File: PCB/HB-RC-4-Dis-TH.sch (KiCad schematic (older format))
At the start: 41 parts, among them J1 FTDI, J2 SHT31, J3 eInk, J4 ISP, J5 Power, Q1 IRLML6346TRBPF, SW1 T1, SW2 T2, SW3 T3, SW4 T4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

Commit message: update pcb
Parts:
- J2: footprint Connector_PinHeader_2.00mm:PinHeader_1x04_P2.00mm_Vertical -> Connector_PinHeader_2.54mm:PinHeader_1x04_P2.54mm_Vertical
- SW1, SW2, SW3, SW4, SW5: footprint Button_Switch_SMD:SW_SPST_PTS645 -> Button_Switch_THT:SW_PUSH_6mm_H5mm
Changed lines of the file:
@@
 F 0 "SW1" H 9930 4300 50  0000 C CNN
 F 1 "T1" H 9930 4210 50  0000 C CNN
-F 2 "Button_Switch_SMD:SW_SPST_PTS645" H 9930 4250 50  0001 C CNN
+F 2 "Button_Switch_THT:SW_PUSH_6mm_H5mm" H 9930 4250 50  0001 C CNN
 F 3 "~" H 9930 4250 50  0001 C CNN
 	1    9930 4050
@@
 F 0 "SW2" H 9570 4400 50  0000 C CNN
 F 1 "T2" H 9570 4310 50  0000 C CNN
-F 2 "Button_Switch_SMD:SW_SPST_PTS645" H 9570 4350 50  0001 C CNN
+F 2 "Button_Switch_THT:SW_PUSH_6mm_H5mm" H 9570 4350 50  0001 C CNN
 F 3 "~" H 9570 4350 50  0001 C CNN
 	1    9570 4150
@@
 F 0 "SW3" H 9230 4500 50  0000 C CNN
 F 1 "T3" H 9230 4410 50  0000 C CNN
-F 2 "Button_Switch_SMD:SW_SPST_PTS645" H 9230 4450 50  0001 C CNN
+F 2 "Button_Switch_THT:SW_PUSH_6mm_H5mm" H 9230 4450 50  0001 C CNN
 F 3 "~" H 9230 4450 50  0001 C CNN
 	1    9230 4250
@@
 F 0 "SW4" H 8900 4610 50  0000 C CNN
 F 1 "T4" H 8900 4510 50  0000 C CNN
-F 2 "Button_Switch_SMD:SW_SPST_PTS645" H 8900 4550 50  0001 C CNN
+F 2 "Button_Switch_THT:SW_PUSH_6mm_H5mm" H 8900 4550 50  0001 C CNN
 F 3 "~" H 8900 4550 50  0001 C CNN
 	1    8900 4350
@@
 F 0 "SW5" H 8830 5300 50  0000 C CNN
 F 1 "Config" H 8830 5210 50  0000 C CNN
-F 2 "Button_Switch_SMD:SW_SPST_PTS645" H 8830 5250 50  0001 C CNN
+F 2 "Button_Switch_THT:SW_PUSH_6mm_H5mm" H 8830 5250 50  0001 C CNN
 F 3 "~" H 8830 5250 50  0001 C CNN
 	1    8830 5050
@@
 F 0 "J2" H 1580 1562 50  0000 L CNN
 F 1 "SHT31" H 1580 1471 50  0000 L CNN
-F 2 "Connector_PinHeader_2.00mm:PinHeader_1x04_P2.00mm_Vertical" H 1500 1570 50  0001 C CNN
+F 2 "Connector_PinHeader_2.54mm:PinHeader_1x04_P2.54mm_Vertical" H 1500 1570 50  0001 C CNN
 F 3 "~" H 1500 1570 50  0001 C CNN
 	1    1500 1570

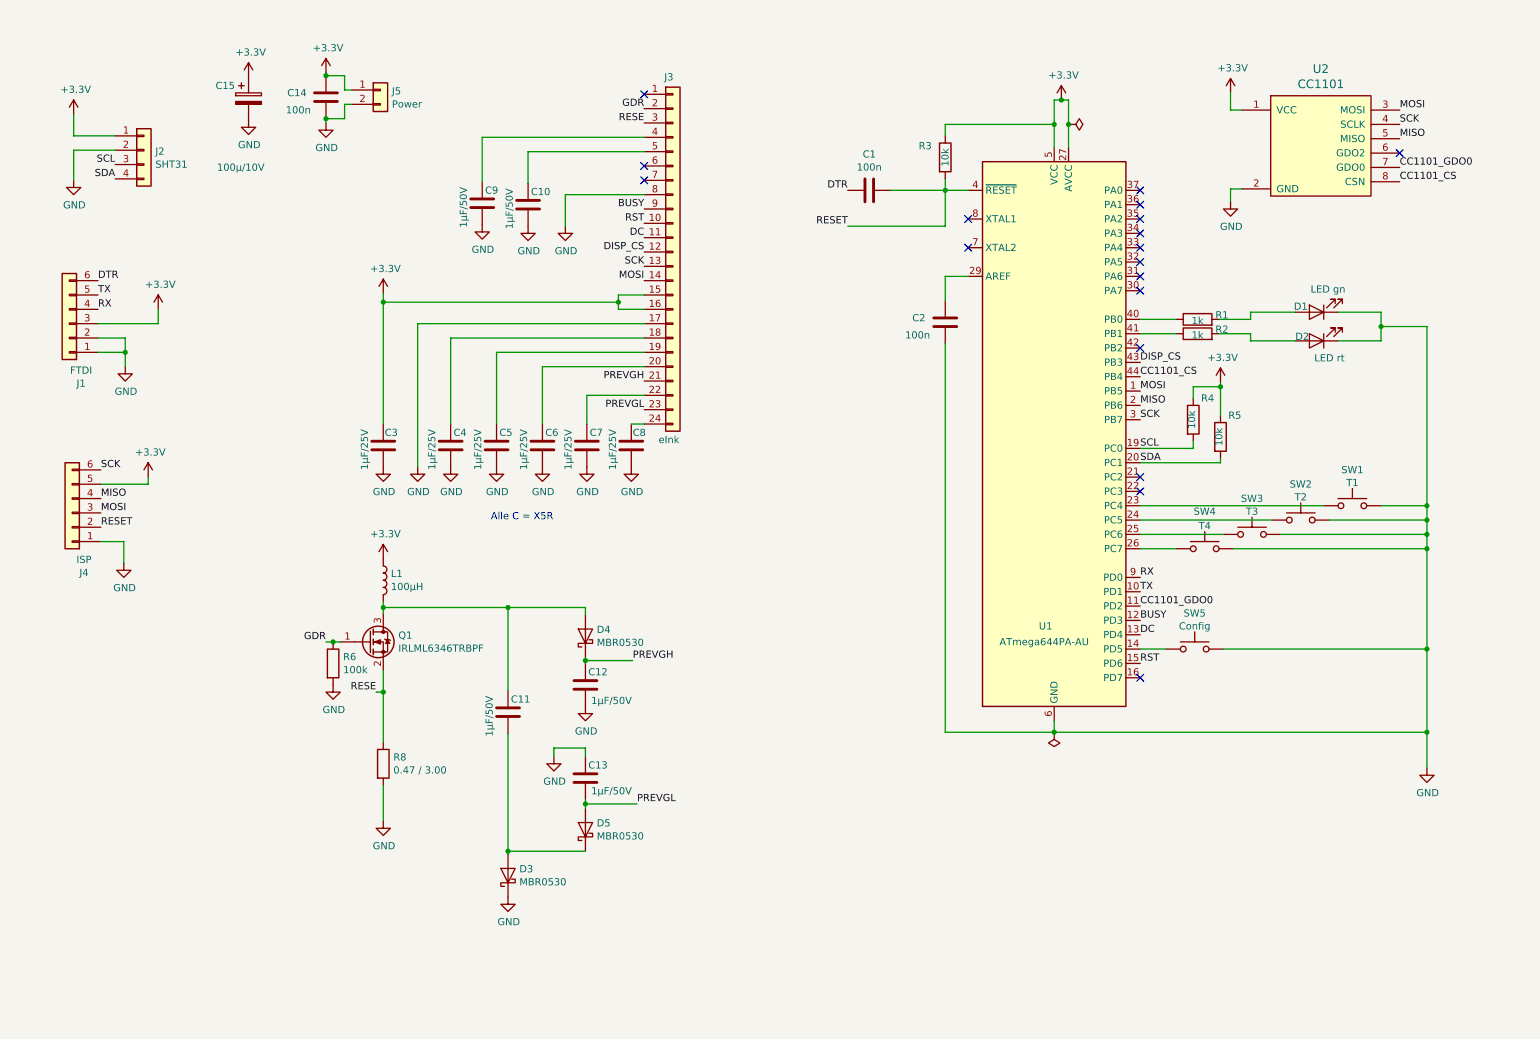
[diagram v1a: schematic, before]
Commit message: update pcb v1.1 (added decoupling capacitors)
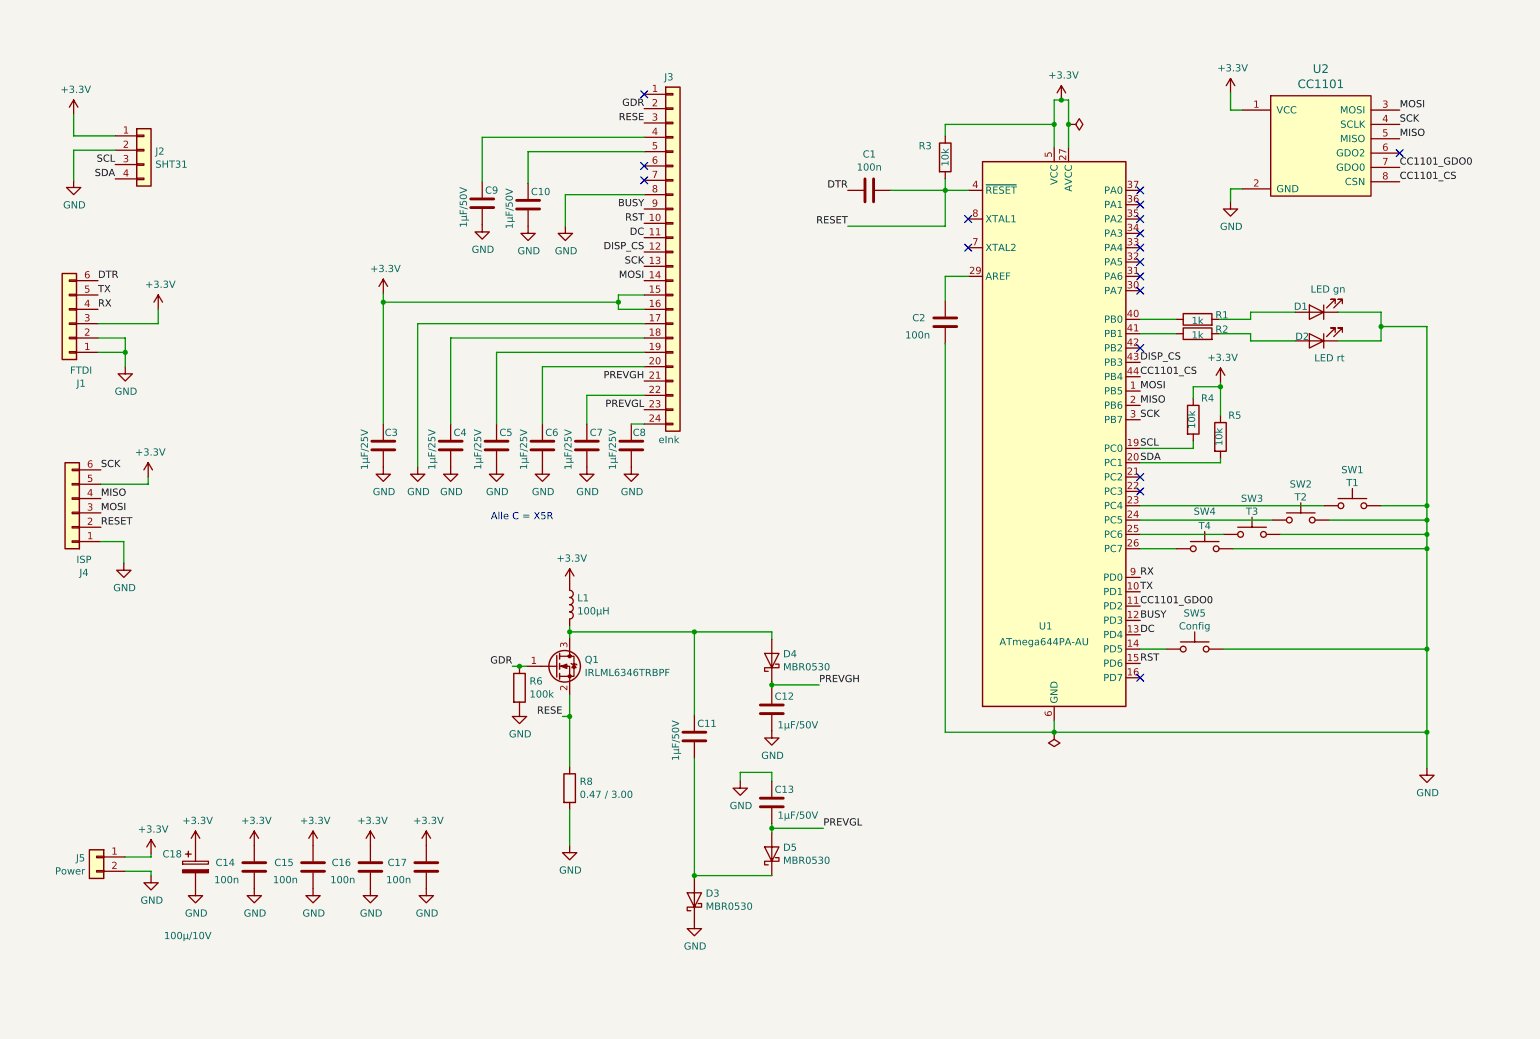
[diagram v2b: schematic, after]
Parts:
- added C15, C16, C17: 100n, Capacitor_SMD:C_0805_2012Metric_Pad1.15x1.40mm_HandSolder, symbol Device:C
- renumbered C15 to C18
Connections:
- net +3V3: now also C15.1, C16.1, C17.1
- net GND: now also C15.2, C16.2, C17.2
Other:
- moved on the sheet: C11, C12, C13, C14, C18, D3, D4, D5, J5, L1, Q1, R6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

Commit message: changed resistor values
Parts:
- D1: value LED gn -> LED rt
- D2: value LED rt -> gn
- R1, R2: value 1k -> 330
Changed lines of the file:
@@
 P 8850 2750
 F 0 "R1" V 8880 2580 50  0000 C CNN
-F 1 "1k" V 8840 2750 50  0000 C CNN
+F 1 "330" V 8840 2750 50  0000 C CNN
 F 2 "Resistor_SMD:R_0805_2012Metric_Pad1.15x1.40mm_HandSolder" V 8780 2750 50  0001 C CNN
 F 3 "~" H 8850 2750 50  0001 C CNN
@@
 P 8850 2850
 F 0 "R2" V 8880 2680 50  0000 C CNN
-F 1 "1k" V 8840 2850 50  0000 C CNN
+F 1 "330" V 8840 2850 50  0000 C CNN
 F 2 "Resistor_SMD:R_0805_2012Metric_Pad1.15x1.40mm_HandSolder" V 8780 2850 50  0001 C CNN
 F 3 "~" H 8850 2850 50  0001 C CNN
@@
 P 9680 2700
 F 0 "D1" H 9790 2660 50  0000 C CNN
-F 1 "LED gn" H 9600 2540 50  0000 C CNN
+F 1 "LED rt" H 9600 2540 50  0000 C CNN
 F 2 "LED_SMD:LED_0805_2012Metric_Pad1.15x1.40mm_HandSolder" H 9680 2700 50  0001 C CNN
 F 3 "~" H 9680 2700 50  0001 C CNN
@@
 P 9680 2900
 F 0 "D2" H 9780 2870 50  0000 C CNN
-F 1 "LED rt" H 9590 3020 50  0000 C CNN
+F 1 "gn" H 9590 3020 50  0000 C CNN
 F 2 "LED_SMD:LED_0805_2012Metric_Pad1.15x1.40mm_HandSolder" H 9680 2900 50  0001 C CNN
 F 3 "~" H 9680 2900 50  0001 C CNN

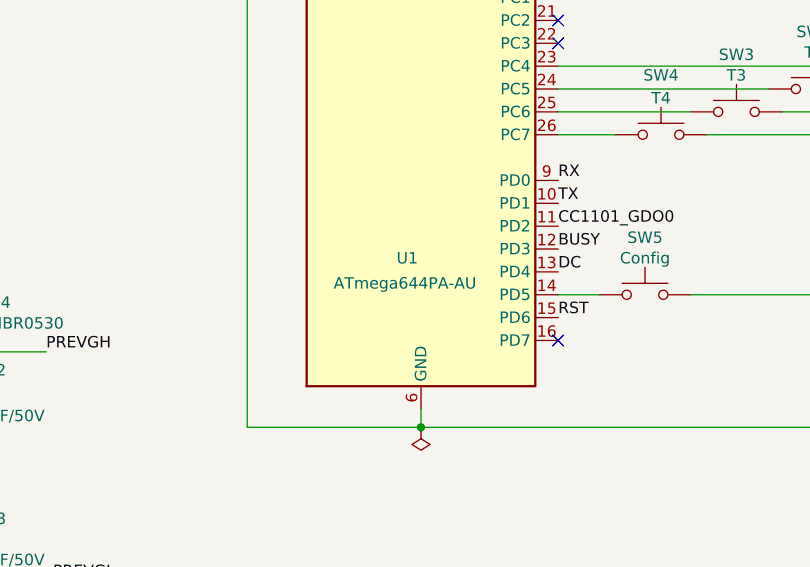
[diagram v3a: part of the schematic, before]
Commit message: change AVR to 1284P
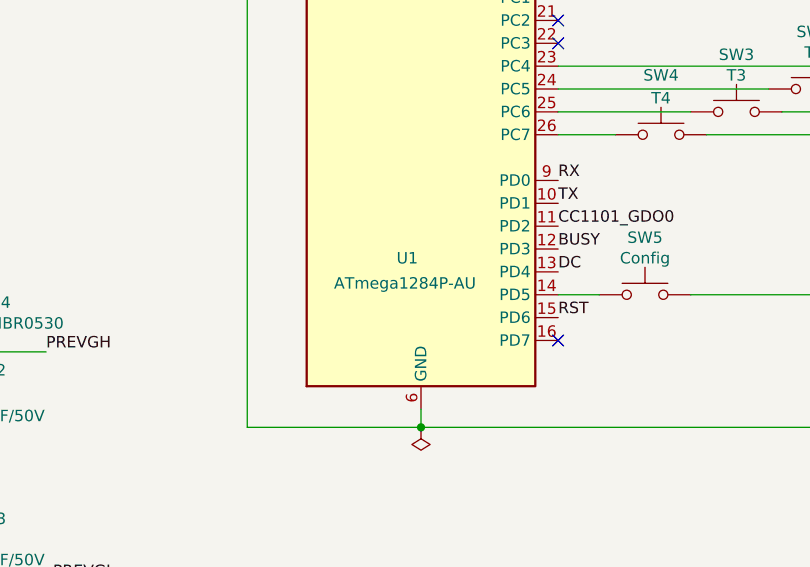
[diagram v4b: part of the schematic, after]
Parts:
- U1: value ATmega644PA-AU -> ATmega1284P-AU
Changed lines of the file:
@@
 P 7850 3550
 F 0 "U1" H 7790 2210 50  0000 C CNN
-F 1 "ATmega644PA-AU" H 7780 2100 50  0000 C CNN
+F 1 "ATmega1284P-AU" H 7780 2100 50  0000 C CNN
 F 2 "Package_QFP:TQFP-44_10x10mm_P0.8mm" H 7850 3550 50  0001 C CIN
 F 3 "http://ww1.microchip.com/downloads/en/DeviceDoc/Atmel-8272-8-bit-AVR-microcontroller-ATmega164A_PA-324A_PA-644A_PA-1284_P_datasheet.pdf" H 7850 3550 50  0001 C CNN

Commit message: update
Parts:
- added C19, C20: 10/6, Capacitor_SMD:C_0805_2012Metric_Pad1.15x1.40mm_HandSolder, symbol Device:C
- added D6: LED bl, LED_SMD:LED_0805_2012Metric_Pad1.15x1.40mm_HandSolder, symbol Device:LED
- added J6: Batt, Connector_PinHeader_2.54mm:PinHeader_1x02_P2.54mm_Vertical, symbol Connector_Generic:Conn_01x02
- added JP1: SolderJumper_3_Open, Jumper:SolderJumper-3_P1.3mm_Open_RoundedPad1.0x1.5mm, symbol Jumper:SolderJumper_3_Open
- added R10: 100k, Resistor_SMD:R_0805_2012Metric_Pad1.15x1.40mm_HandSolder, symbol Device:R
- added R11: 1k, Resistor_SMD:R_0805_2012Metric_Pad1.15x1.40mm_HandSolder, symbol Device:R
- added R12: 240, Resistor_SMD:R_0805_2012Metric_Pad1.15x1.40mm_HandSolder, symbol Device:R
- added R7: 2k2, Resistor_SMD:R_0805_2012Metric_Pad1.15x1.40mm_HandSolder, symbol Device:R
- added R9: 470k, Resistor_SMD:R_0805_2012Metric_Pad1.15x1.40mm_HandSolder, symbol Device:R
- added U3: MCP1703T-3302E/CB, Package_TO_SOT_SMD:SOT-23, symbol Regulator_Linear:MCP1703A-1202_SOT23
- added U4: MCP73831T-2ACI/OT, Package_TO_SOT_SMD:SOT-23-5, symbol Battery_Management:MCP73831-2-OT
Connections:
- net +3V3: now also C20.1, JP1.1 (A), U3.2 (VO); no longer J5.1 (Pin_1)
- net GND: now also C19.2, C20.2, J6.2 (Pin_2), R7.2, U3.1 (GND), U4.2 (VSS)
- net B_ACTIVATION: now reaches U1.21 (PC2)
- net B_ACTIVATION: now also R10.1
- net B_CHARGING: now reaches U1.22 (PC3)
- net B_CHARGING: now also R11.2
- net B_MEASURE: now reaches U1.37 (PA0)
- net B_MEASURE: now also R10.2, R9.1
- new net: J5.1 (Pin_1), JP1.2 (C)
- new net: R11.1, R12.1, U4.1 (STAT)
- new net: D6.2 (A), JP1.3 (B), U4.4 (VDD)
- new net: R7.1, U4.5 (PROG)
- new net: D6.1 (K), R12.2
- new net +BATT: C19.1, J6.1 (Pin_1), R9.2, U3.3 (VI), U4.3 (VBAT)
- no-connect marks 18 -> 15
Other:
- moved on the sheet: C10, C14, C15, C16, C17, C18, C3, C4, C5, C6, C7, C8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

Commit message: update
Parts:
- added R13: 100k, Resistor_SMD:R_0805_2012Metric_Pad1.15x1.40mm_HandSolder, symbol Device:R
- added U5: PC357, Package_SO:SO-4_4.4x3.6mm_P2.54mm, symbol Isolator:SFH617A-1X007T
- C19, C20: value 10/6 -> 10/10
- R11: value 1k -> 680
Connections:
- net +3V3: now also R13.1
- net B_CHARGING: now also R13.2, U5.4; no longer R11.2
- net GND: now also U5.3
- net at D6.2 (A), JP1.3 (B), U4.4 (VDD): now also U5.1
- new net: R11.2, U5.2
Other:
- moved on the sheet: C19, C20, J6, R11, U3

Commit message: update pcb V2.1
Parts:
- U1: symbol MCU_Microchip_ATmega:ATmega644PA-AU -> MCU_Microchip_ATmega:ATmega1284P-AU
- renumbered J1 to FTDI1, J4 to ISP1, J2 to SHT31
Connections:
- net B_MEASURE: now also U1.34 (PA3); no longer U1.37 (PA0)
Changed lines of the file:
@@
 NoConn ~ 8450 1950
 NoConn ~ 8450 2050
-NoConn ~ 8450 2150
 NoConn ~ 8450 2250
 NoConn ~ 8450 2350
@@
 RX
 $Comp
-L Connector_Generic:Conn_01x04 J2
+L Connector_Generic:Conn_01x04 SHT31
 U 1 1 5F30CE44
 P 1380 1250
-F 0 "J2" H 1460 1242 50  0000 L CNN
-F 1 "SHT31" H 1460 1151 50  0000 L CNN
+F 0 "SHT31" H 1460 1242 50  0000 L CNN
+F 1 "SHT31" H 1460 1151 50  0001 L CNN
 F 2 "Connector_PinHeader_2.54mm:PinHeader_1x04_P2.54mm_Vertical" H 1380 1250 50  0001 C CNN
 F 3 "~" H 1380 1250 50  0001 C CNN
@@
 	2040 1460 2230 1460
 $Comp
-L Connector_Generic:Conn_01x06 J1
+L Connector_Generic:Conn_01x06 FTDI1
 U 1 1 5F3355F4
 P 1840 1360
-F 0 "J1" H 1758 1777 50  0000 C CNN
-F 1 "FTDI" H 1758 1686 50  0000 C CNN
+F 0 "FTDI1" H 1758 1777 50  0000 C CNN
+F 1 "FTDI" H 1758 1686 50  0001 C CNN
 F 2 "Connector_PinHeader_2.54mm:PinHeader_1x06_P2.54mm_Vertical" H 1840 1360 50  0001 C CNN
 F 3 "~" H 1840 1360 50  0001 C CNN
@@
 $EndComp
 $Comp
-L Connector_Generic:Conn_01x06 J4
+L Connector_Generic:Conn_01x06 ISP1
 U 1 1 5F3363EF
 P 2840 1350
-F 0 "J4" H 2758 1767 50  0000 C CNN
-F 1 "ISP" H 2758 1676 50  0000 C CNN
+F 0 "ISP1" H 2758 1767 50  0000 C CNN
+F 1 "ISP" H 2758 1676 50  0001 C CNN
 F 2 "additional:PinPads_ISP" H 2840 1350 50  0001 C CNN
 F 3 "~" H 2840 1350 50  0001 C CNN
@@
 $EndComp
 $Comp
-L MCU_Microchip_ATmega:ATmega644PA-AU U1
+L MCU_Microchip_ATmega:ATmega1284P-AU U1
 U 1 1 5F2D0377
 P 7850 3550
@@
 Text Label 8450 3850 0    50   ~ 0
 B_ACTIVATION
-Text Label 8450 1850 0    50   ~ 0
+Text Label 8450 2150 0    50   ~ 0
 B_MEASURE
 Text Label 3290 4490 0    50   ~ 0
@@
 Wire Wire Line
 	3210 4490 3210 4580
+NoConn ~ 8450 1850
 $EndSCHEMATC

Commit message: update pcb
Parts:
- added R8-2: 1, Resistor_SMD:R_0805_2012Metric_Pad1.15x1.40mm_HandSolder, symbol Device:R
- D6: value LED bl -> LED wt
- L1: value 100µH -> 68µH
- R12: value 240 -> 1k
- R7: value 2k2 -> 4k7
- R8-1: renamed from R8; value 0.47 / 3.00 -> 1
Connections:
- net GND: now also R8-2.2
- net RESE: now also R8-2.1
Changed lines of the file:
@@
 P 4470 4740
 F 0 "L1" H 4523 4786 50  0000 L CNN
-F 1 "100µH" H 4523 4695 50  0000 L CNN
+F 1 "68µH" H 4523 4695 50  0000 L CNN
 F 2 "Inductor_SMD:L_Wuerth_MAPI-3012" H 4470 4740 50  0001 C CNN
 F 3 "~" H 4470 4740 50  0001 C CNN
@@
 Connection ~ 4470 5520
 $Comp
-L Device:R R8
+L Device:R R8-1
 U 1 1 5F3FE6D2
 P 4470 6020
-F 0 "R8" H 4540 6066 50  0000 L CNN
-F 1 "0.47 / 3.00" H 4540 5975 50  0000 L CNN
+F 0 "R8-1" V 4380 5920 50  0000 L CNN
+F 1 "1" H 4450 6020 50  0000 L CNN
 F 2 "Resistor_SMD:R_0805_2012Metric_Pad1.15x1.40mm_HandSolder" V 4400 6020 50  0001 C CNN
 F 3 "~" H 4470 6020 50  0001 C CNN
@@
 $EndComp
 Wire Wire Line
-	4470 6170 4470 6420
-Wire Wire Line
-	4470 5520 4470 5870
+	4470 6170 4470 6270
+Wire Wire Line
+	4470 5520 4470 5750
 $Comp
 L Device:C C14
@@
 P 1100 5200
 F 0 "R7" H 910 5250 50  0000 L CNN
-F 1 "2k2" H 860 5160 50  0000 L CNN
+F 1 "4k7" H 860 5160 50  0000 L CNN
 F 2 "Resistor_SMD:R_0805_2012Metric_Pad1.15x1.40mm_HandSolder" V 1030 5200 50  0001 C CNN
 F 3 "~" H 1100 5200 50  0001 C CNN
@@
 P 2230 5010
 F 0 "R12" V 2310 4950 50  0000 L CNN
-F 1 "240" V 2220 4940 50  0000 L CNN
+F 1 "1k" V 2220 4940 50  0000 L CNN
 F 2 "Resistor_SMD:R_0805_2012Metric_Pad1.15x1.40mm_HandSolder" V 2160 5010 50  0001 C CNN
 F 3 "~" H 2230 5010 50  0001 C CNN
@@
 P 2380 4680
 F 0 "D6" V 2500 4880 50  0000 C CNN
-F 1 "LED bl" V 2400 4880 50  0000 C CNN
+F 1 "LED wt" V 2400 4880 50  0000 C CNN
 F 2 "LED_SMD:LED_0805_2012Metric_Pad1.15x1.40mm_HandSolder" H 2380 4680 50  0001 C CNN
 F 3 "~" H 2380 4680 50  0001 C CNN
@@
 	3210 4490 3210 4580
 NoConn ~ 8450 1850
+$Comp
+L Device:R R8-2
+U 1 1 5F741DFD
+P 4250 6020
+F 0 "R8-2" V 4170 5920 50  0000 L CNN
+F 1 "1" H 4220 6020 50  0000 L CNN
+F 2 "Resistor_SMD:R_0805_2012Metric_Pad1.15x1.40mm_HandSolder" V 4180 6020 50  0001 C CNN
+F 3 "~" H 4250 6020 50  0001 C CNN
+	1    4250 6020
+	1    0    0    -1
+$EndComp
+Wire Wire Line
+	4250 6170 4250 6270
+Wire Wire Line
+	4250 6270 4470 6270
+Connection ~ 4470 6270
+Wire Wire Line
+	4470 6270 4470 6420
+Wire Wire Line
+	4250 5870 4250 5750
+Wire Wire Line
+	4250 5750 4470 5750
+Connection ~ 4470 5750
+Wire Wire Line
+	4470 5750 4470 5870
 $EndSCHEMATC
